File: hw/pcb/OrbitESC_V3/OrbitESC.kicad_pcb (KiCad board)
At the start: 8 copper layers, 45.2 x 29.7 mm, 159 parts, among them J1 USB_C_Receptacle_USB2.0, J11 VDC, J12 GND, J13 RX, J2 CANH, J3 TermA, J4 TermB, J5 TermC, J6 GND, J7 CANL, J8 Micro_SD_Card_Det2, J9 TX, Q1 MCAC100N08YA-TP, Q2 MCAC100N08YA-TP, Q3 MCAC100N08YA-TP, Q4 MCAC100N08YA-TP, Q5 MCAC100N08YA-TP, Q6 MCAC100N08YA-TP, Q7 2N7002, SW1 Reset, SW2 DFU, U1 TLE9250X, U13 TLV9051IDBVR, U14 TLV9051IDBVR, U2 AT25SF128A-SHB-T, U3 STM32F446RETx, U4 TLV9051IDBVR, U5 DRV8300DRGER, U6 TLV9051IDBVR, U7 AP62200Z6-7, U8 AP2171W, U9 AP2120, X1 ASE-24MHz

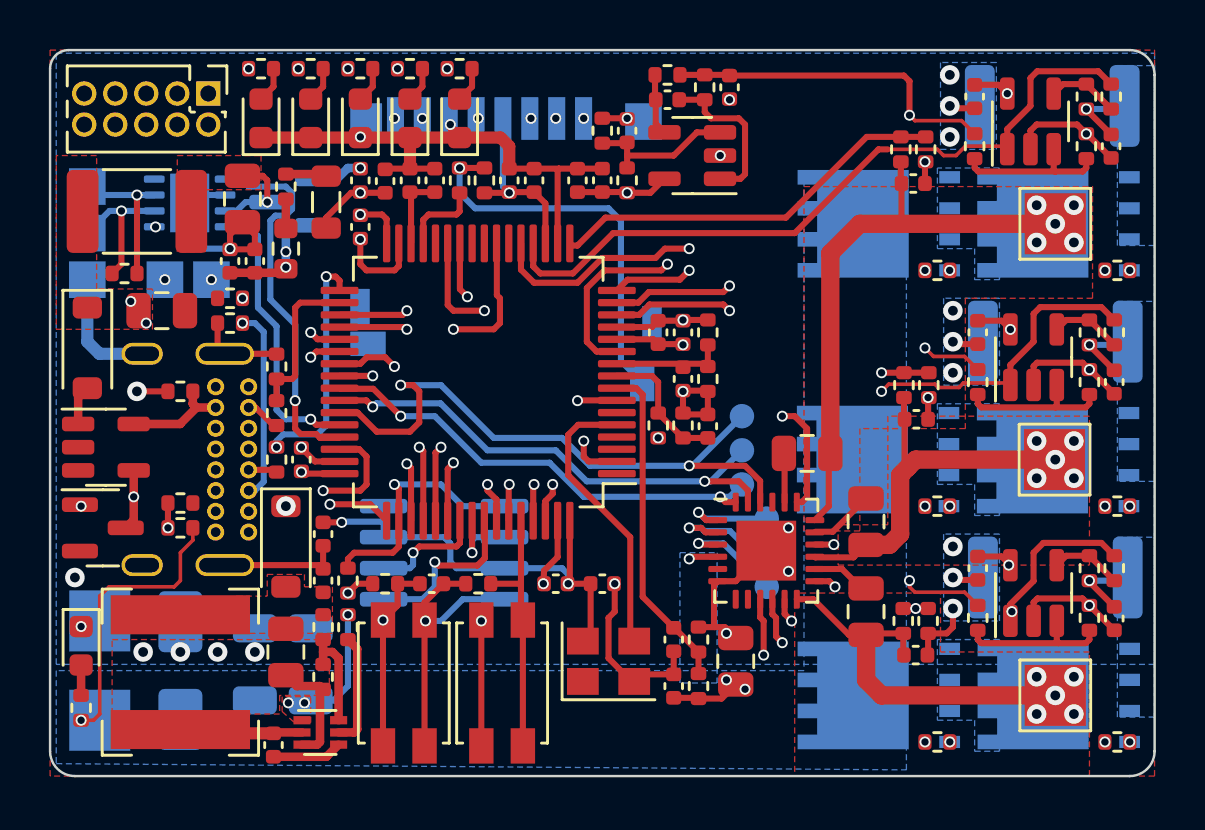
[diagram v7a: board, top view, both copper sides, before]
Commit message: PCB cleanup. BOM checks.
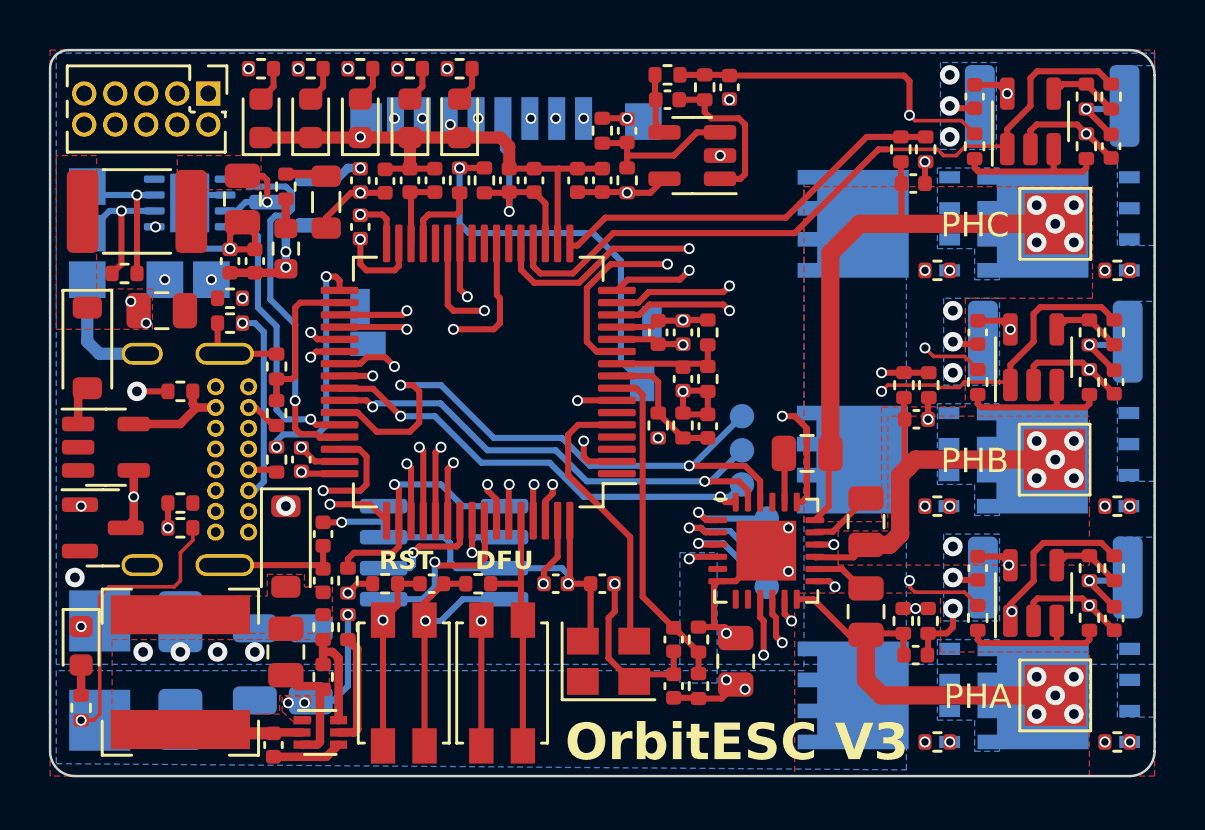
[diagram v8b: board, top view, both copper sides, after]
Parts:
- R45, R49, R51: value 18k -> 39k
- R46, R48, R50: value 1k -> 5.1k
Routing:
- net +3.3V: track 41.4 -> 42.9 mm
- added copper zone on In3.Cu, net +3.3V
- added copper zone on In2.Cu, net GND
- added copper zone on In5.Cu, net GND
- removed copper zone on In6.Cu, net +3.3V
- removed copper zone on In1.Cu, net GND
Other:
- board text added: "+18v/10A Max"
- board text added: "DFU"
- board text added: "FAULT|ARM|HB|CAN|USB"
- board text added: "OrbitESC V3"
- board text added: "PHA"
- board text added: "PHB"
- board text added: "PHC"
- board text added: "RST"
- board text added: "VDC"
